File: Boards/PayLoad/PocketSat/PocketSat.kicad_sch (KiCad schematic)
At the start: 71 parts, among them J20 DX07S016JA1R1500, J3 MEM2061-01-188-00-A_REVA, J5 BM03B-SRSS-TBLFSN, Q1 BC857CMB_315, U1 HDC2080DMBR, U4 LPS22DFTR, U5 W25Q128JVSIQ TR, U6 BMP581, U8 ST1L05APU33R

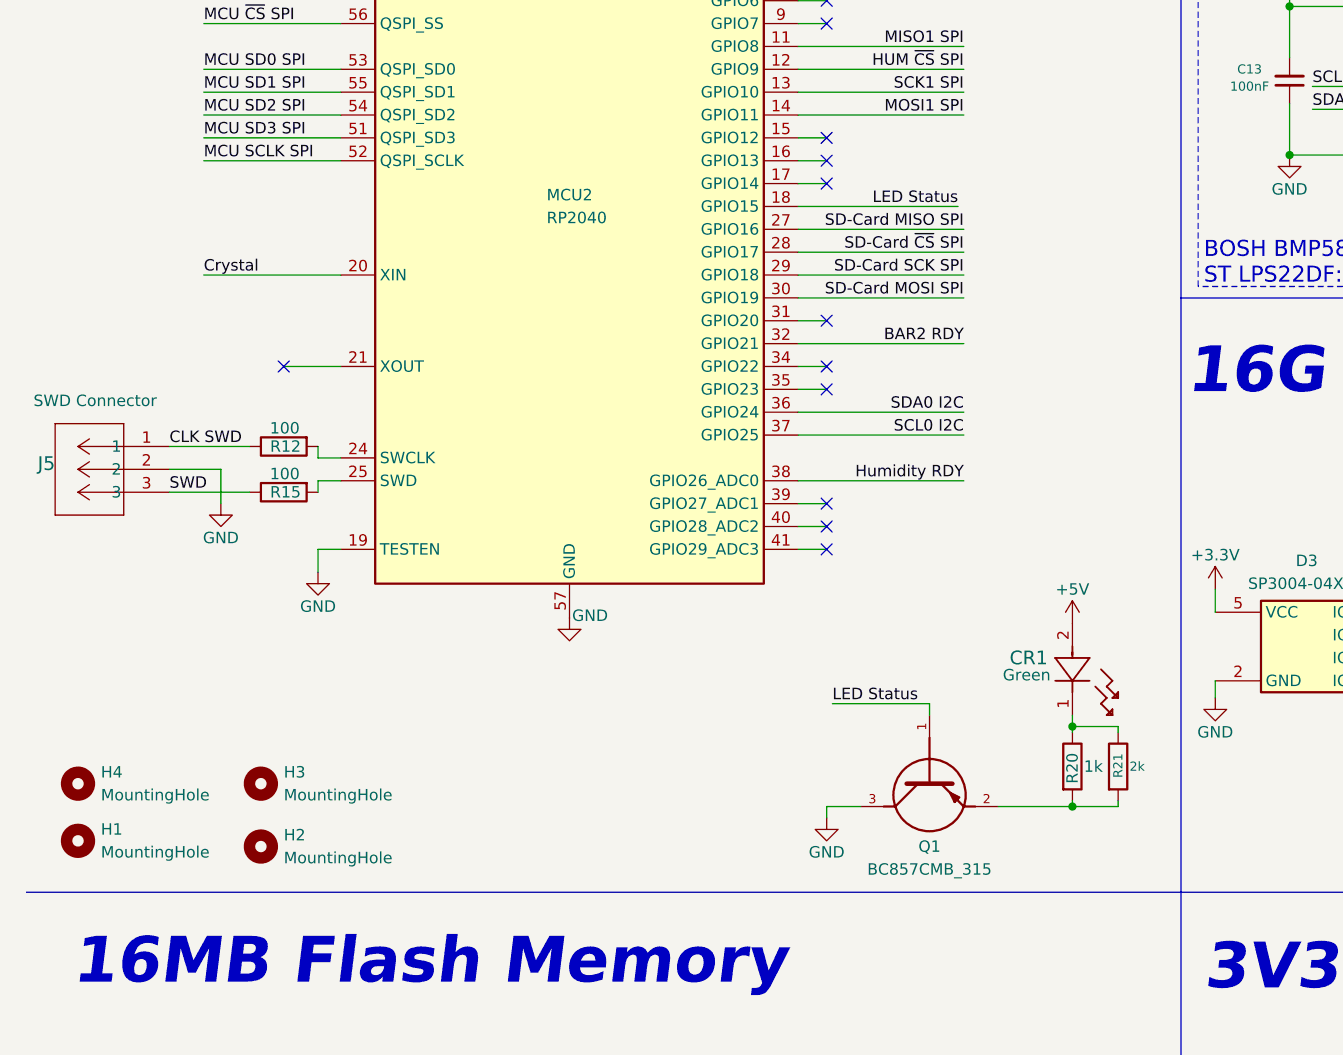
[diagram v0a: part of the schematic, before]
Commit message: Adicionei um driver novo de leds e outras correçoes
Adicionei um novo driver de leds substitui pelo velho e corrigimos mais
erros de DRC
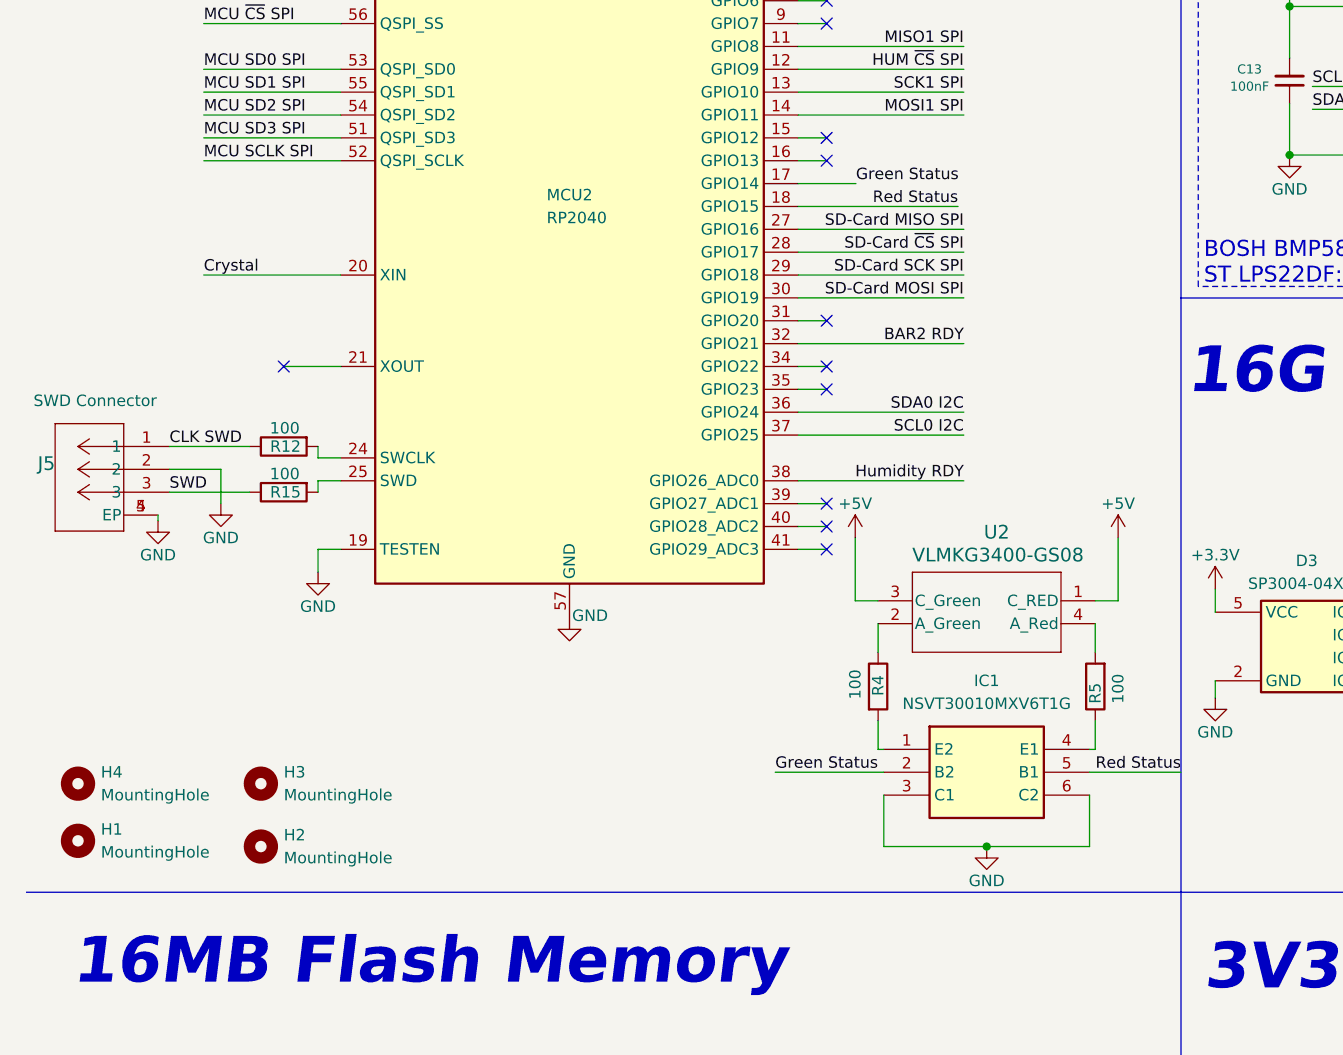
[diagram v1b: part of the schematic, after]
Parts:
- removed CR1: VLMC3100-GS08, LED-Green_VLMC3100-GS08:LED_PLCC_VSMB, symbol GreenLED__VLMC3100-GS08:VLMC3100-GS08
- removed Q1: BC857CMB_315, PNP_BC857CMB_315:TRANS_PMZB550UNEYL, symbol BC857CMB_315:BC857CMB_315
- removed R20: 1k, Resistor-0402:RES_0402, symbol Device:R
- removed R21: 2k, Resistor-0402:RES_0402, symbol Device:R
- added IC1: NSVT30010MXV6T1G, 2 PNP:SOT-563_1P3X1P7_ONS, symbol NSVT30010MXV6T1G:NSVT30010MXV6T1G
- added R4, R5: 100, Resistor-0603:RES_0603, symbol Device:R
- added U2: VLMKG3400-GS08, VLMKG3400-GS08:SMT_00-GS08_VIS, symbol VLMKG3400-GS08:VLMKG3400-GS08
- J5: footprint SWD_Con:CONN_BM03B-SRSS-TBLFSN_JST -> CONN_BM03B-SRSS-TBLFSN_JST
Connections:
- net +5V: now also U2.1 (C_RED), U2.3 (C_Green)
- net GND: now also J5.4 (EP), J5.5 (EP), IC1.3 (C1), IC1.6 (C2)
- net Green Status: now reaches MCU2.17 (GPIO14)
- net Green Status: now also IC1.2 (B2)
- net LED Status renamed Red Status
- net Red Status: now also IC1.5 (B1)
- new net: IC1.1 (E2), R4.2
- new net: IC1.4 (E1), R5.1
- new net: R4.1, U2.2 (A_Green)
- new net: R5.2, U2.4 (A_Red)
- no-connect marks 21 -> 20

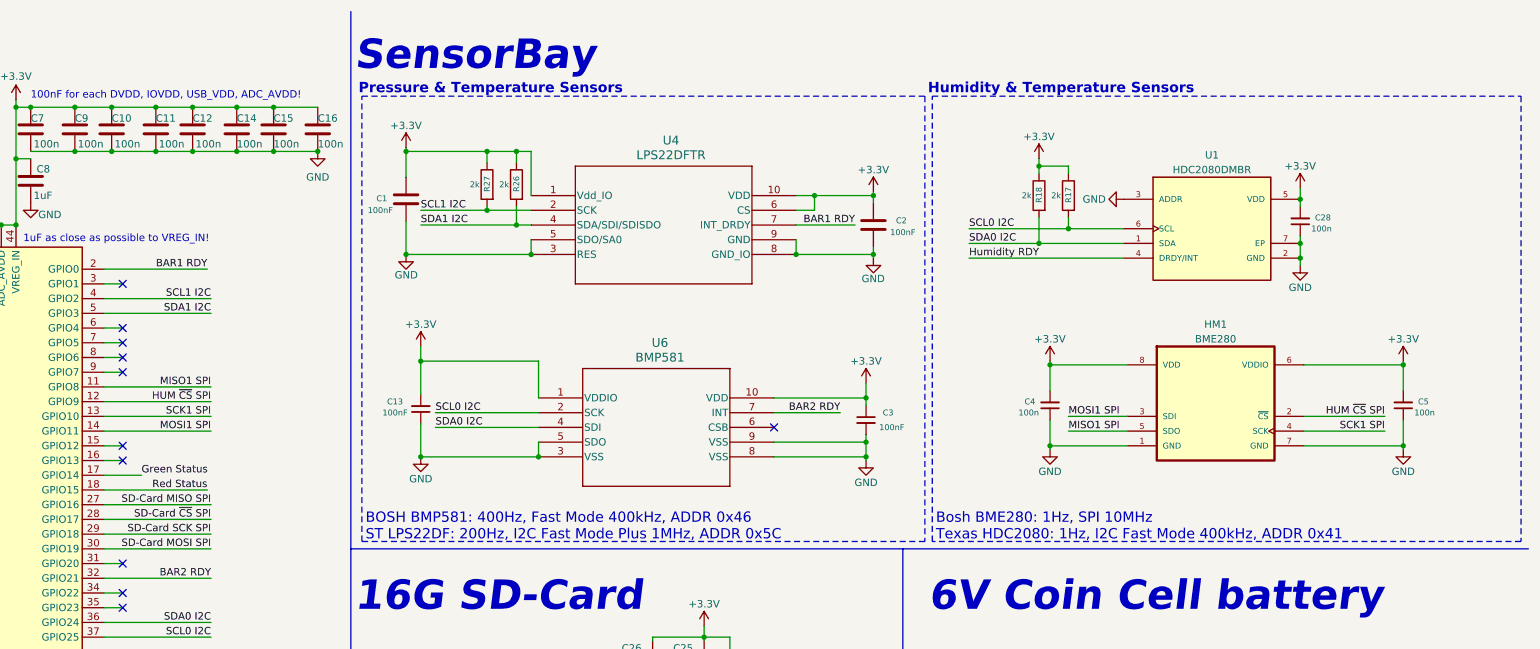
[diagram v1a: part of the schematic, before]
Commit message: OBC, Nav, PocketSat review - SPI and I2C mistakes corrected
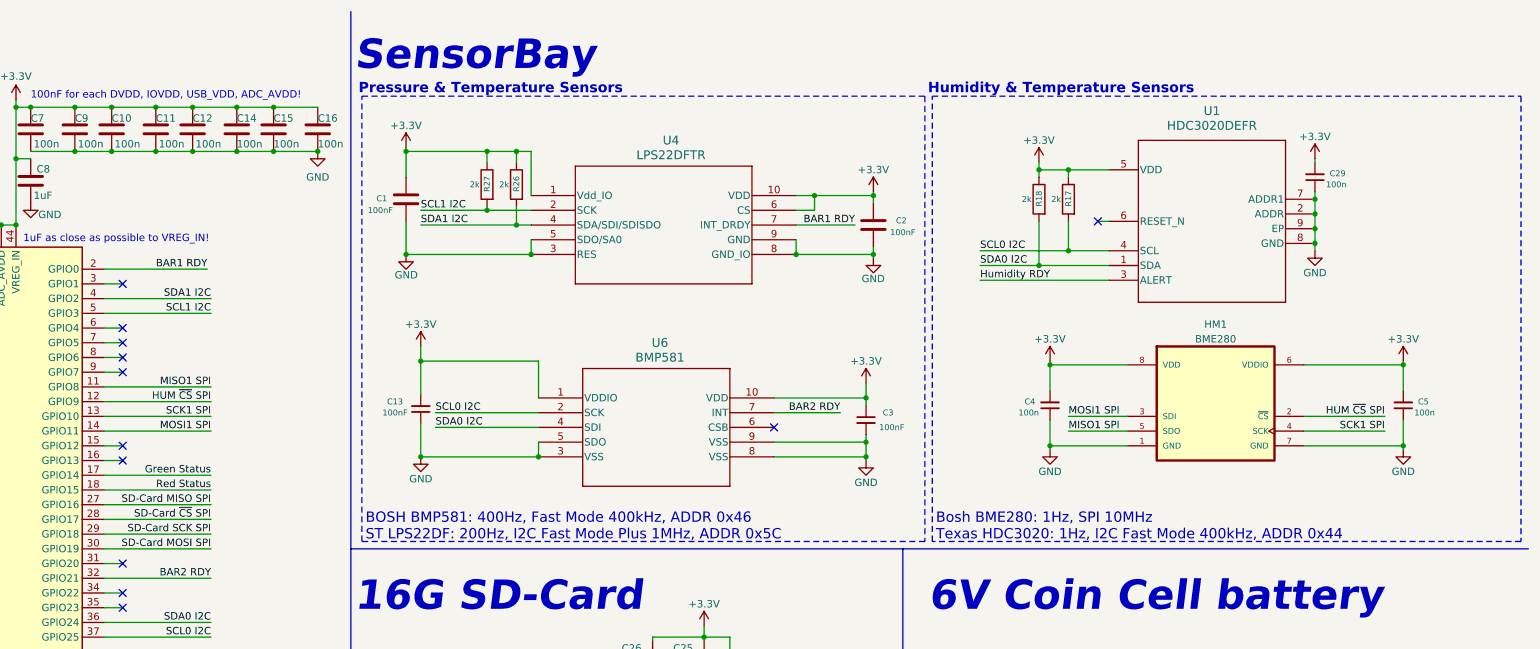
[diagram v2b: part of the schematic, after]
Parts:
- removed C28: 100n, Capacitor-0402:Capacitor_0402, symbol Device:C_Small
- removed U1: HDC2080DMBR, HDC2080DMBR:SON100P300X300X80-7N, symbol HDC2080DMBR:HDC2080DMBR
- added C29: 100n, Capacitor-0402:Capacitor_0402, symbol Device:C_Small
- added U1: HDC3020DEFR, HDC3020DEFR:DEF0008A-IPC_C, symbol HDC3020DEFR:HDC3020DEFR
- J5: footprint CONN_BM03B-SRSS-TBLFSN_JST -> SWD_Con:CONN_BM03B-SRSS-TBLFSN_JST
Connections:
- net +3.3V: now also C29.2, U1.5 (VDD)
- net GND: now also C29.1, U1.2 (ADDR), U1.7 (ADDR1), U1.8 (GND), U1.9 (EP)
- net Humidity RDY: now also U1.3 (ALERT)
- net SCL0 I2C: now also U1.4 (SCL)
- net SCL1 I2C: now also MCU2.5 (GPIO3); no longer MCU2.4 (GPIO2)
- net SDA0 I2C: now also U1.1 (SDA)
- net SDA1 I2C: now also MCU2.4 (GPIO2); no longer MCU2.5 (GPIO3)
- no-connect marks 20 -> 21
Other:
- note added: "Bosh BME280: 1Hz, SPI 10MHz Texas HDC3020: 1Hz, I2C Fast Mode 400kHz, ADDR 0x44"
- note removed: "Bosh BME280: 1Hz, SPI 10MHz Texas HDC2080: 1Hz, I2C Fast Mode 400kHz, ADDR 0x41"
- moved on the sheet: R17, R18
